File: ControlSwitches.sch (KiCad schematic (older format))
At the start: 13 parts, among them J6 Backup, SW1 HAZARD, SW2 CRUISE_SET, SW3 CRUISE, SW4 F/R_SW, SW5 HEADLIGHT_SW, SW6 BACKUP_SW, SW7 TURN_SIGNAL_SW

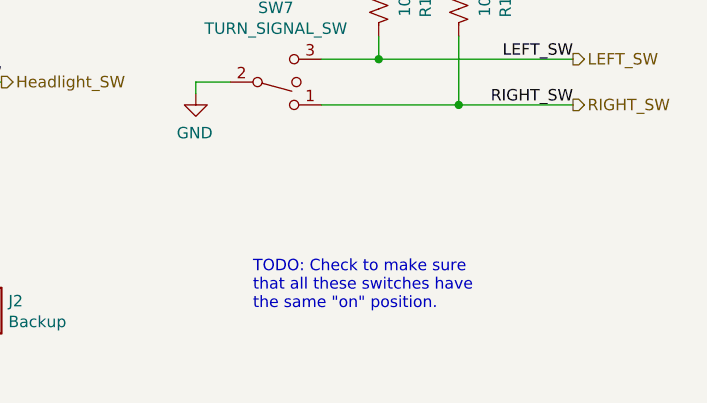
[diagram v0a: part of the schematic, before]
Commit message: Deleted TODO in Switches
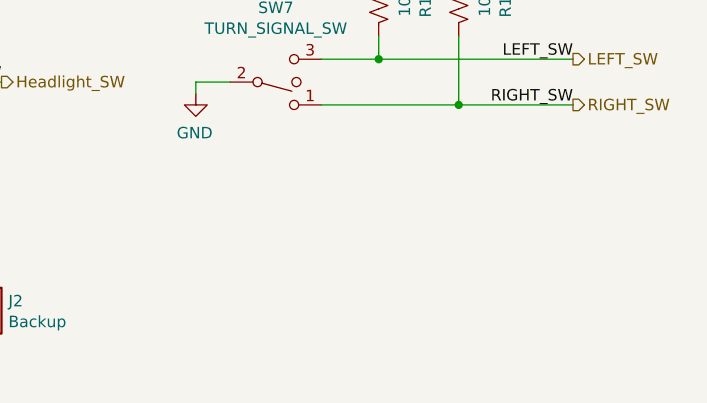
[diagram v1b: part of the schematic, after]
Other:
- note removed: "TODO: Check to make sure\nthat all these switches have\nthe same "on" position."
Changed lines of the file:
@@
 Text Label 6050 5100 2    50   ~ 0
 Backup
-Text Notes 7400 5150 0    50   ~ 0
-TODO: Check to make sure\nthat all these switches have\nthe same "on" position.
 Wire Wire Line
 	5150 4050 5400 4050

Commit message: Resized PCB, changed switches to horizontal, need to organize components
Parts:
- SW1, SW2, SW3, SW4, SW5, SW6, SW7: footprint UTSVT_Connectors:Molex_MicroFit3.0_1x3xP3.00mm_PolarizingPeg_Vertical -> Connector_Molex:Molex_Micro-Fit_3.0_43650-0300_1x03_P3.00mm_Horizontal
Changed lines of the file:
@@
 F 0 "SW2" H 4000 2875 50  0000 C CNN
 F 1 "CRUISE_SET" H 4000 2966 50  0000 C CNN
-F 2 "UTSVT_Connectors:Molex_MicroFit3.0_1x3xP3.00mm_PolarizingPeg_Vertical" H 4000 3200 50  0001 C CNN
+F 2 "Connector_Molex:Molex_Micro-Fit_3.0_43650-0300_1x03_P3.00mm_Horizontal" H 4000 3200 50  0001 C CNN
 F 3 "~" H 4000 3200 50  0001 C CNN
 	1    4000 3200
@@
 F 0 "SW3" H 4000 3825 50  0000 C CNN
 F 1 "CRUISE" H 4000 3916 50  0000 C CNN
-F 2 "UTSVT_Connectors:Molex_MicroFit3.0_1x3xP3.00mm_PolarizingPeg_Vertical" H 4000 4150 50  0001 C CNN
+F 2 "Connector_Molex:Molex_Micro-Fit_3.0_43650-0300_1x03_P3.00mm_Horizontal" H 4000 4150 50  0001 C CNN
 F 3 "~" H 4000 4150 50  0001 C CNN
 	1    4000 4150
@@
 F 0 "SW1" H 3950 4775 50  0000 C CNN
 F 1 "HAZARD" H 3950 4866 50  0000 C CNN
-F 2 "UTSVT_Connectors:Molex_MicroFit3.0_1x3xP3.00mm_PolarizingPeg_Vertical" H 3950 5100 50  0001 C CNN
+F 2 "Connector_Molex:Molex_Micro-Fit_3.0_43650-0300_1x03_P3.00mm_Horizontal" H 3950 5100 50  0001 C CNN
 F 3 "~" H 3950 5100 50  0001 C CNN
 	1    3950 5100
@@
 F 0 "SW7" H 7500 3825 50  0000 C CNN
 F 1 "TURN_SIGNAL_SW" H 7500 3916 50  0000 C CNN
-F 2 "UTSVT_Connectors:Molex_MicroFit3.0_1x3xP3.00mm_PolarizingPeg_Vertical" H 7500 4150 50  0001 C CNN
+F 2 "Connector_Molex:Molex_Micro-Fit_3.0_43650-0300_1x03_P3.00mm_Horizontal" H 7500 4150 50  0001 C CNN
 F 3 "~" H 7500 4150 50  0001 C CNN
 	1    7500 4150
@@
 F 0 "SW4" H 5600 2875 50  0000 C CNN
 F 1 "F/R_SW" H 5600 2966 50  0000 C CNN
-F 2 "UTSVT_Connectors:Molex_MicroFit3.0_1x3xP3.00mm_PolarizingPeg_Vertical" H 5600 3200 50  0001 C CNN
+F 2 "Connector_Molex:Molex_Micro-Fit_3.0_43650-0300_1x03_P3.00mm_Horizontal" H 5600 3200 50  0001 C CNN
 F 3 "~" H 5600 3200 50  0001 C CNN
 	1    5600 3200
@@
 F 0 "SW6" H 5600 4775 50  0000 C CNN
 F 1 "BACKUP_SW" H 5600 4866 50  0000 C CNN
-F 2 "UTSVT_Connectors:Molex_MicroFit3.0_1x3xP3.00mm_PolarizingPeg_Vertical" H 5600 5100 50  0001 C CNN
+F 2 "Connector_Molex:Molex_Micro-Fit_3.0_43650-0300_1x03_P3.00mm_Horizontal" H 5600 5100 50  0001 C CNN
 F 3 "~" H 5600 5100 50  0001 C CNN
 	1    5600 5100
@@
 F 0 "SW5" H 5600 3825 50  0000 C CNN
 F 1 "HEADLIGHT_SW" H 5600 3916 50  0000 C CNN
-F 2 "UTSVT_Connectors:Molex_MicroFit3.0_1x3xP3.00mm_PolarizingPeg_Vertical" H 5600 4150 50  0001 C CNN
+F 2 "Connector_Molex:Molex_Micro-Fit_3.0_43650-0300_1x03_P3.00mm_Horizontal" H 5600 4150 50  0001 C CNN
 F 3 "~" H 5600 4150 50  0001 C CNN
 	1    5600 4150

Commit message: Changed all switch connectors to horizontal, board dimensions to 2.5in by 4.5in, and started board layout
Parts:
- J6: footprint UTSVT_Connectors:Molex_MicroFit3.0_1x2xP3.00mm_PolarizingPeg_Vertical -> Connector_Molex:Molex_Micro-Fit_3.0_43650-0200_1x02_P3.00mm_Horizontal
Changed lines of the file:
@@
 F 0 "J2" H 6330 5092 50  0000 L CNN
 F 1 "Backup" H 6330 5001 50  0000 L CNN
-F 2 "UTSVT_Connectors:Molex_MicroFit3.0_1x2xP3.00mm_PolarizingPeg_Vertical" H 6250 5100 50  0001 C CNN
+F 2 "Connector_Molex:Molex_Micro-Fit_3.0_43650-0200_1x02_P3.00mm_Horizontal" H 6250 5100 50  0001 C CNN
 F 3 "~" H 6250 5100 50  0001 C CNN
 	1    6250 5100

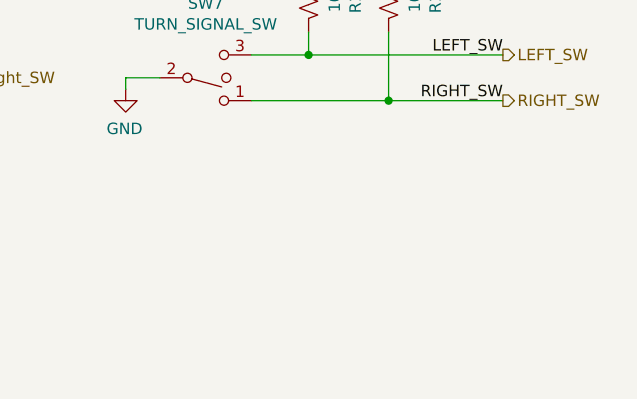
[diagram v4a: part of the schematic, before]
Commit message: Added Regen switch, deleted RSVD LED
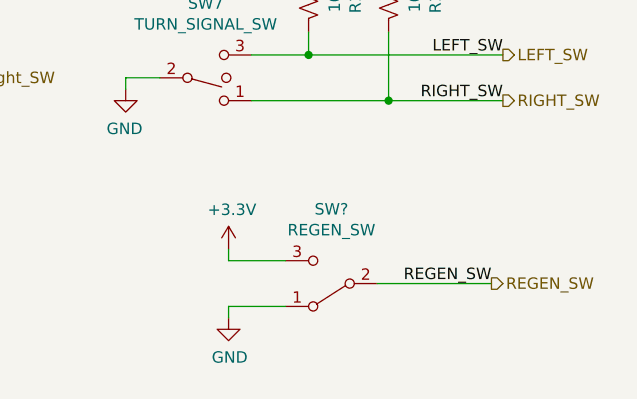
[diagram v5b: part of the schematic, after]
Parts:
- added SW?: REGEN_SW, Connector_Molex:Molex_Micro-Fit_3.0_43650-0300_1x03_P3.00mm_Horizontal, symbol Switch:SW_SPDT
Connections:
- net +3V3: now also SW?.3 (C)
- net GND: now also SW?.1 (A)
- new net REGEN_SW: SW?.2 (B)
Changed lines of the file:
@@
 Text HLabel 8800 4250 2    50   Output ~ 0
 RIGHT_SW
+$Comp
+L Switch:SW_SPDT SW?
+U 1 1 5FC0BDC6
+P 8050 5050
+AR Path="/5FC0BDC6" Ref="SW?"  Part="1"
+AR Path="/5F958945/5FC0BDC6" Ref="SW?"  Part="1"
+AR Path="/5F78B3EB/5FC0BDC6" Ref="SW?"  Part="1"
+F 0 "SW?" H 8050 4725 50  0000 C CNN
+F 1 "REGEN_SW" H 8050 4816 50  0000 C CNN
+F 2 "Connector_Molex:Molex_Micro-Fit_3.0_43650-0300_1x03_P3.00mm_Horizontal" H 8050 5050 50  0001 C CNN
+F 3 "~" H 8050 5050 50  0001 C CNN
+	1    8050 5050
+	-1   0    0    1
+$EndComp
+$Comp
+L power:+3.3V #PWR?
+U 1 1 5FC0BDCC
+P 7600 4900
+AR Path="/5FC0BDCC" Ref="#PWR?"  Part="1"
+AR Path="/5F958945/5FC0BDCC" Ref="#PWR?"  Part="1"
+AR Path="/5F78B3EB/5FC0BDCC" Ref="#PWR?"  Part="1"
+F 0 "#PWR?" H 7600 4750 50  0001 C CNN
+F 1 "+3.3V" H 7615 5073 50  0000 C CNN
+F 2 "" H 7600 4900 50  0001 C CNN
+F 3 "" H 7600 4900 50  0001 C CNN
+	1    7600 4900
+	1    0    0    -1
+$EndComp
+Wire Wire Line
+	7600 4900 7600 4950
+$Comp
+L power:GND #PWR?
+U 1 1 5FC0BDD3
+P 7600 5200
+AR Path="/5FC0BDD3" Ref="#PWR?"  Part="1"
+AR Path="/5F958945/5FC0BDD3" Ref="#PWR?"  Part="1"
+AR Path="/5F78B3EB/5FC0BDD3" Ref="#PWR?"  Part="1"
+F 0 "#PWR?" H 7600 4950 50  0001 C CNN
+F 1 "GND" H 7605 5027 50  0000 C CNN
+F 2 "" H 7600 5200 50  0001 C CNN
+F 3 "" H 7600 5200 50  0001 C CNN
+	1    7600 5200
+	1    0    0    -1
+$EndComp
+Wire Wire Line
+	7600 5200 7600 5150
+Wire Wire Line
+	7600 5150 7850 5150
+Wire Wire Line
+	8250 5050 8750 5050
+Text Label 8750 5050 2    50   ~ 0
+REGEN_SW
+Wire Wire Line
+	7600 4950 7850 4950
+Text HLabel 8750 5050 2    50   Output ~ 0
+REGEN_SW
 $EndSCHEMATC

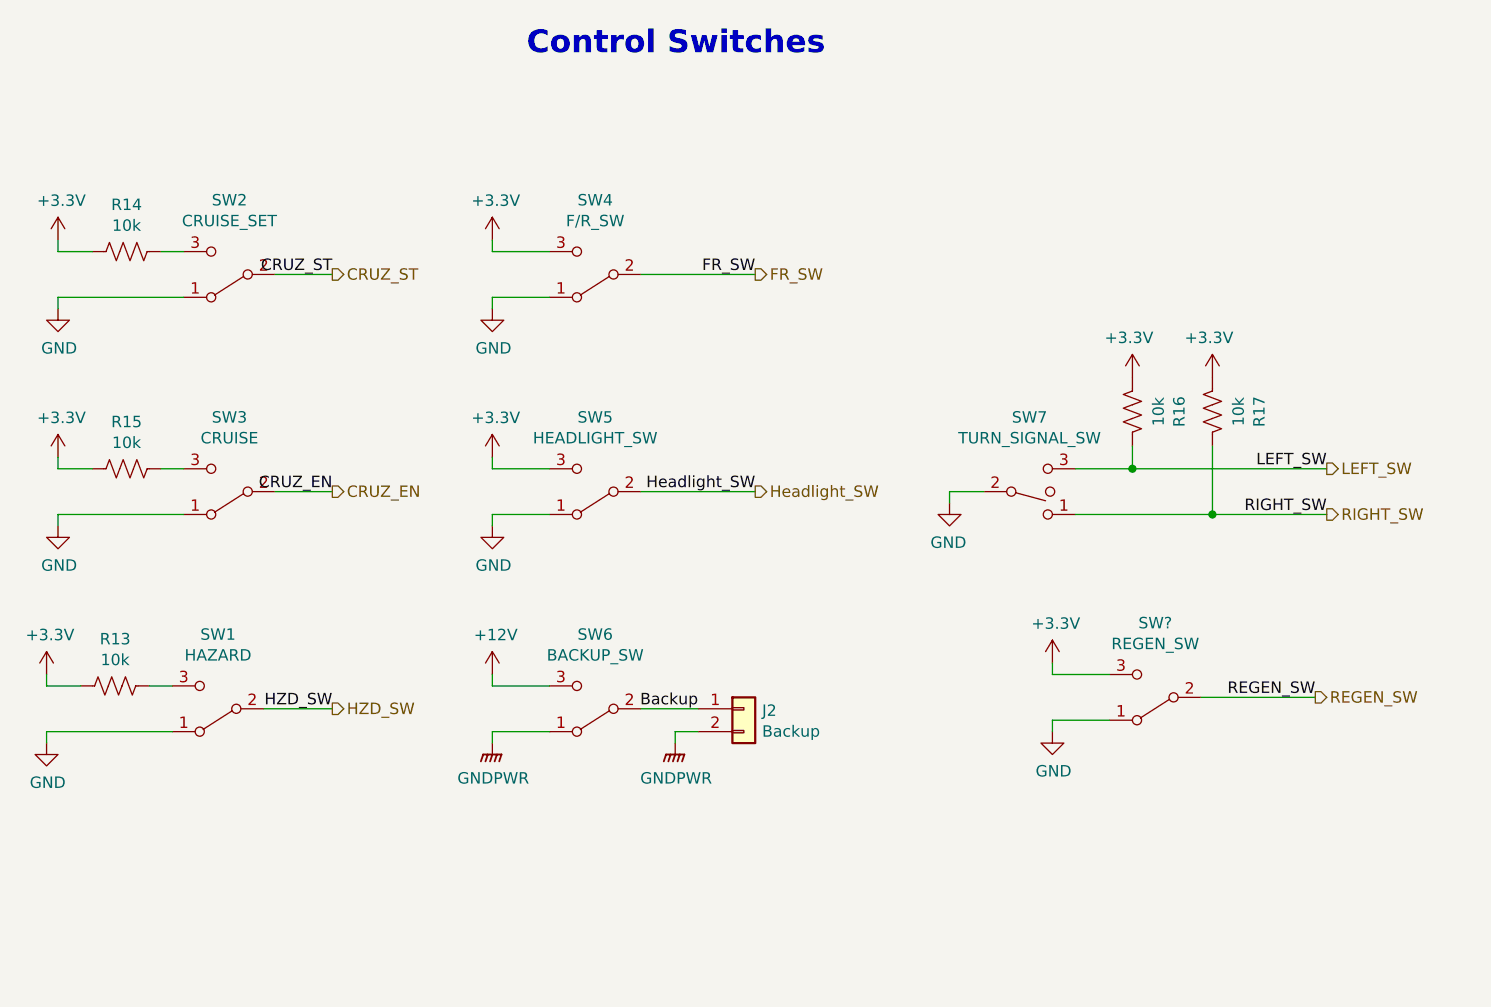
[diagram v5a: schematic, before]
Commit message: Started placing routes, did not finish
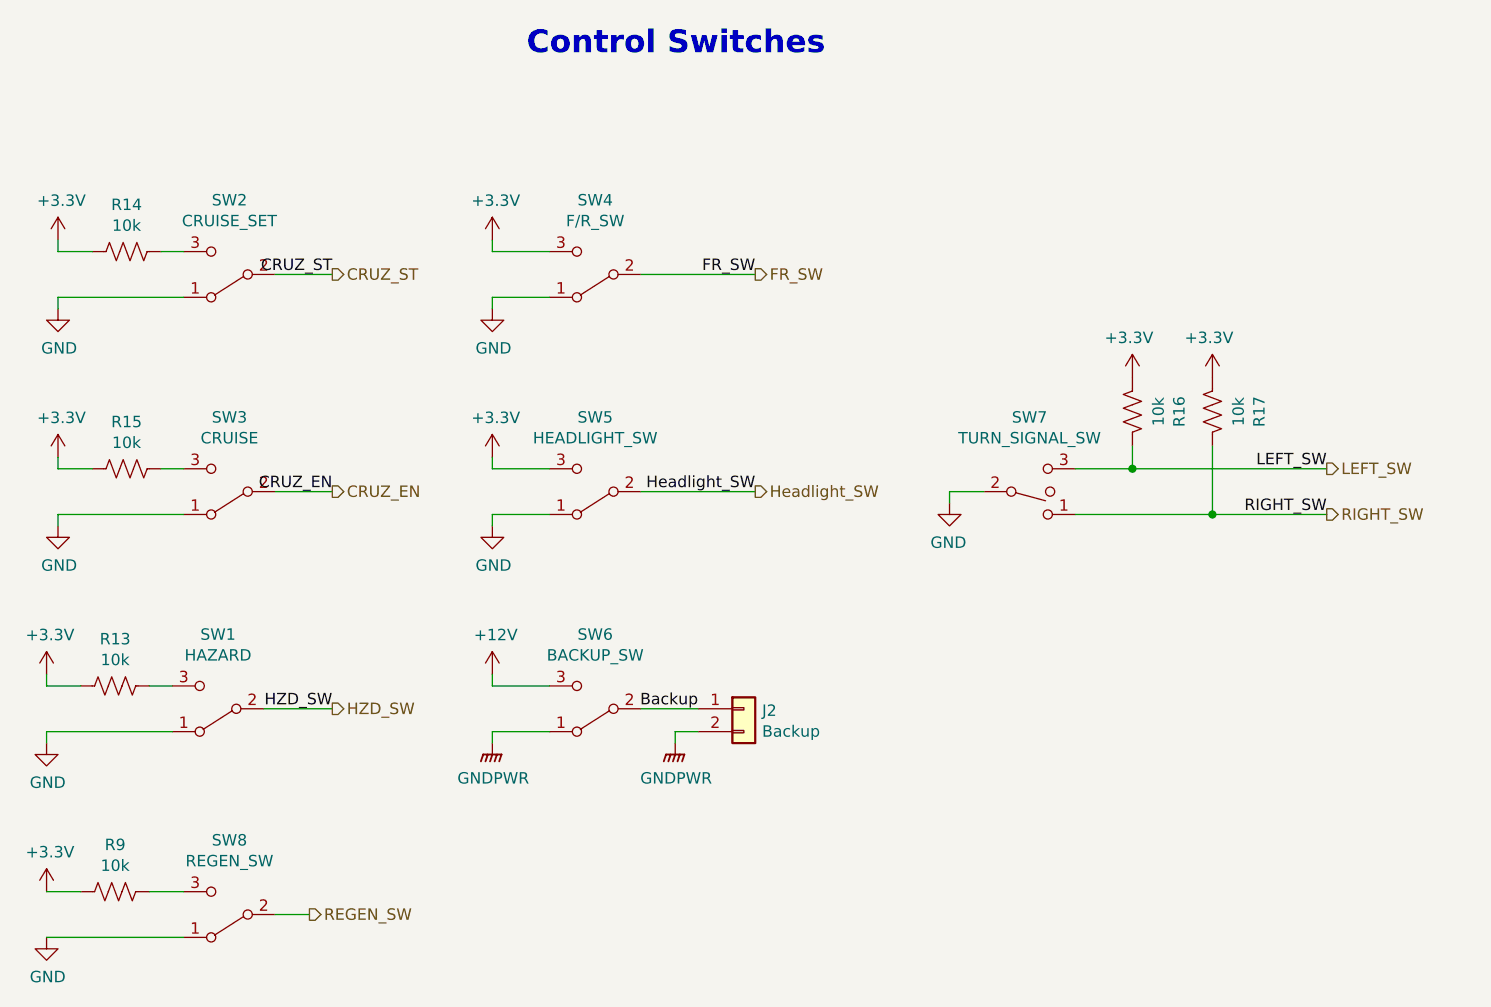
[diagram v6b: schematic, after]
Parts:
- removed SW?: REGEN_SW, Connector_Molex:Molex_Micro-Fit_3.0_43650-0300_1x03_P3.00mm_Horizontal, symbol Switch:SW_SPDT
- added R9: 10k, Resistor_SMD:R_0805_2012Metric, symbol Device:R_US
- added SW8: REGEN_SW, Connector_Molex:Molex_Micro-Fit_3.0_43650-0300_1x03_P3.00mm_Horizontal, symbol Switch:SW_SPDT
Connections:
- net +3V3: now also R9.2
- net GND: now also SW8.1 (A)
- net REGEN_SW: now also SW8.2 (B)
- new net: R9.1, SW8.3 (C)
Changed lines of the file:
@@
 RIGHT_SW
 $Comp
-L Switch:SW_SPDT SW?
-U 1 1 5FC0BDC6
-P 8050 5050
-AR Path="/5FC0BDC6" Ref="SW?"  Part="1"
-AR Path="/5F958945/5FC0BDC6" Ref="SW?"  Part="1"
-AR Path="/5F78B3EB/5FC0BDC6" Ref="SW?"  Part="1"
-F 0 "SW?" H 8050 4725 50  0000 C CNN
-F 1 "REGEN_SW" H 8050 4816 50  0000 C CNN
-F 2 "Connector_Molex:Molex_Micro-Fit_3.0_43650-0300_1x03_P3.00mm_Horizontal" H 8050 5050 50  0001 C CNN
-F 3 "~" H 8050 5050 50  0001 C CNN
-	1    8050 5050
+L power:GND #PWR012
+U 1 1 5FC25956
+P 3200 6100
+F 0 "#PWR012" H 3200 5850 50  0001 C CNN
+F 1 "GND" H 3205 5927 50  0000 C CNN
+F 2 "" H 3200 6100 50  0001 C CNN
+F 3 "" H 3200 6100 50  0001 C CNN
+	1    3200 6100
+	1    0    0    -1
+$EndComp
+$Comp
+L power:+3.3V #PWR011
+U 1 1 5FC25ECF
+P 3200 5900
+F 0 "#PWR011" H 3200 5750 50  0001 C CNN
+F 1 "+3.3V" H 3215 6073 50  0000 C CNN
+F 2 "" H 3200 5900 50  0001 C CNN
+F 3 "" H 3200 5900 50  0001 C CNN
+	1    3200 5900
+	1    0    0    -1
+$EndComp
+$Comp
+L Switch:SW_SPDT SW8
+U 1 1 5FC26A8C
+P 4000 6000
+F 0 "SW8" H 4000 5675 50  0000 C CNN
+F 1 "REGEN_SW" H 4000 5766 50  0000 C CNN
+F 2 "Connector_Molex:Molex_Micro-Fit_3.0_43650-0300_1x03_P3.00mm_Horizontal" H 4000 6000 50  0001 C CNN
+F 3 "~" H 4000 6000 50  0001 C CNN
+	1    4000 6000
 	-1   0    0    1
 $EndComp
 $Comp
-L power:+3.3V #PWR?
-U 1 1 5FC0BDCC
-P 7600 4900
-AR Path="/5FC0BDCC" Ref="#PWR?"  Part="1"
-AR Path="/5F958945/5FC0BDCC" Ref="#PWR?"  Part="1"
-AR Path="/5F78B3EB/5FC0BDCC" Ref="#PWR?"  Part="1"
-F 0 "#PWR?" H 7600 4750 50  0001 C CNN
-F 1 "+3.3V" H 7615 5073 50  0000 C CNN
-F 2 "" H 7600 4900 50  0001 C CNN
-F 3 "" H 7600 4900 50  0001 C CNN
-	1    7600 4900
-	1    0    0    -1
+L Device:R_US R9
+U 1 1 5FC2B876
+P 3500 5900
+F 0 "R9" V 3295 5900 50  0000 C CNN
+F 1 "10k" V 3386 5900 50  0000 C CNN
+F 2 "Resistor_SMD:R_0805_2012Metric" V 3540 5890 50  0001 C CNN
+F 3 "~" H 3500 5900 50  0001 C CNN
+	1    3500 5900
+	0    1    1    0
 $EndComp
 Wire Wire Line
-	7600 4900 7600 4950
-$Comp
-L power:GND #PWR?
-U 1 1 5FC0BDD3
-P 7600 5200
-AR Path="/5FC0BDD3" Ref="#PWR?"  Part="1"
-AR Path="/5F958945/5FC0BDD3" Ref="#PWR?"  Part="1"
-AR Path="/5F78B3EB/5FC0BDD3" Ref="#PWR?"  Part="1"
-F 0 "#PWR?" H 7600 4950 50  0001 C CNN
-F 1 "GND" H 7605 5027 50  0000 C CNN
-F 2 "" H 7600 5200 50  0001 C CNN
-F 3 "" H 7600 5200 50  0001 C CNN
-	1    7600 5200
-	1    0    0    -1
-$EndComp
+	3650 5900 3800 5900
 Wire Wire Line
-	7600 5200 7600 5150
+	3200 5900 3350 5900
 Wire Wire Line
-	7600 5150 7850 5150
-Wire Wire Line
-	8250 5050 8750 5050
-Text Label 8750 5050 2    50   ~ 0
+	3200 6100 3800 6100
+Text HLabel 4350 6000 2    50   Output ~ 0
 REGEN_SW
 Wire Wire Line
-	7600 4950 7850 4950
-Text HLabel 8750 5050 2    50   Output ~ 0
-REGEN_SW
+	4200 6000 4350 6000
 $EndSCHEMATC

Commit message: Finished connections and changed F/W switch, but hierarchial labels on schematic need to be fixed
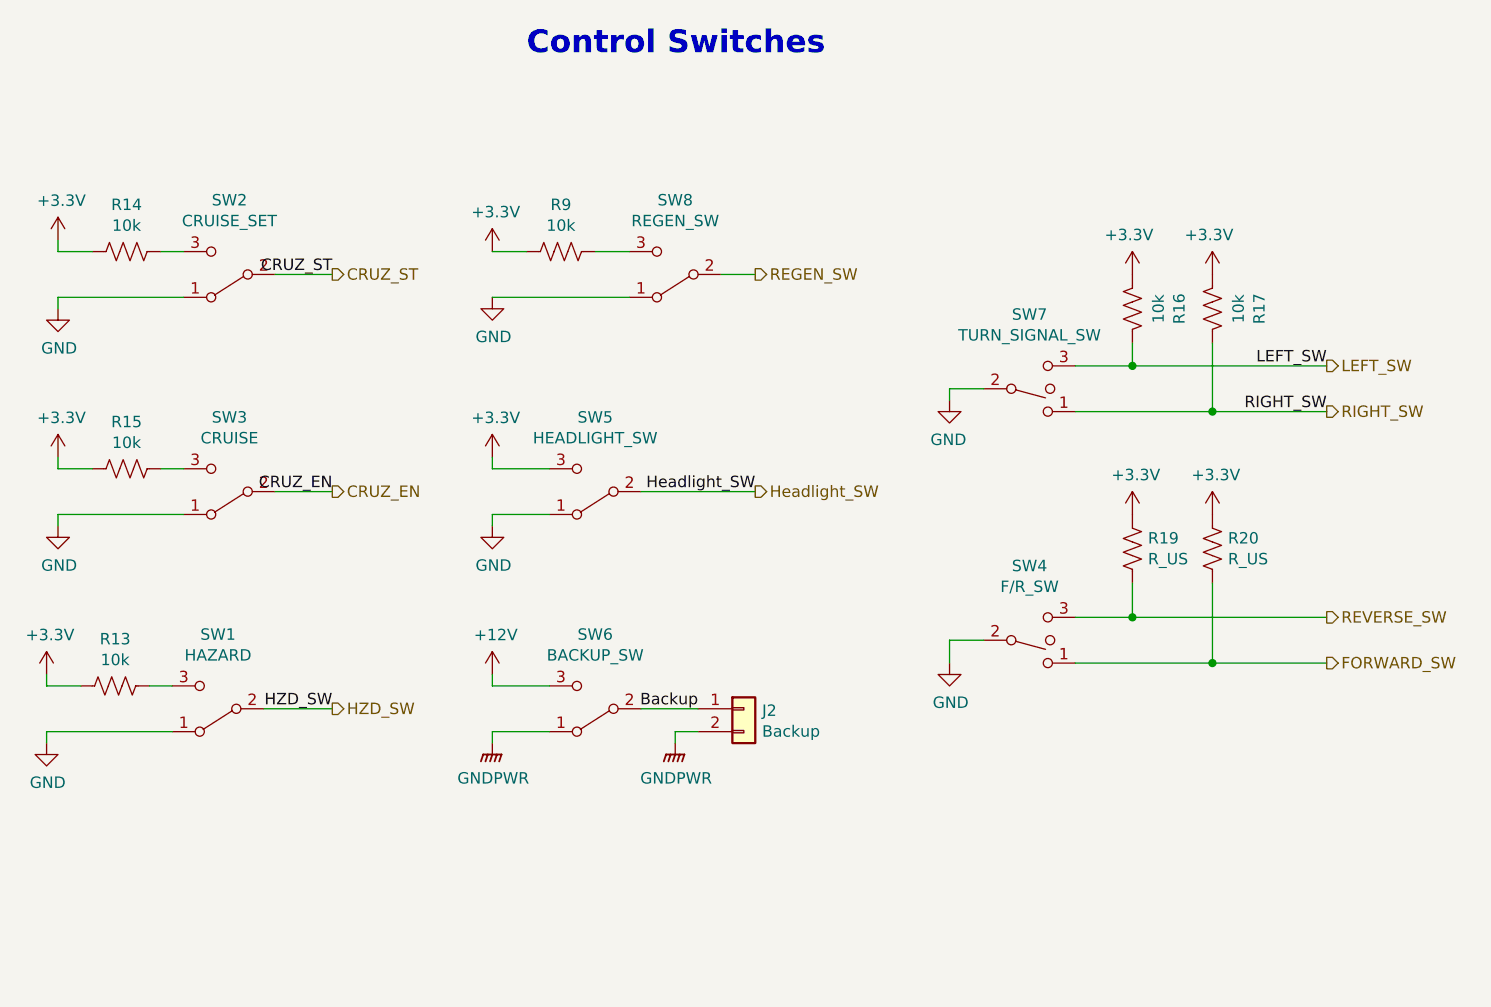
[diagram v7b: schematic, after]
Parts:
- removed SW4: F/R_SW, Connector_Molex:Molex_Micro-Fit_3.0_43650-0300_1x03_P3.00mm_Horizontal, symbol Switch:SW_SPDT
- added R19, R20: R_US, symbol Device:R_US
- added SW4: F/R_SW, symbol Switch:SW_SPDT_MSM
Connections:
- net +3V3: now also R19.1, R20.1
- net GND: now also SW4.2
- new net FORWARD_SW: R20.2, SW4.1
- new net REVERSE_SW: R19.2, SW4.3
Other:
- moved on the sheet: R16, R17, R9, SW7, SW8
